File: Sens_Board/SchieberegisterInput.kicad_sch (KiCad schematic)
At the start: 18 parts, among them U4 74HC165

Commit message: Senssoard Firsat LAyout start
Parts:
- C10: renamed from C76; footprint Capacitor_SMD:C_0603_1608Metric -> Capacitor_SMD:C_0402_1005Metric
- C11: renamed from C88; footprint Capacitor_SMD:C_0603_1608Metric -> Capacitor_SMD:C_0402_1005Metric
- C12: renamed from C100; footprint Capacitor_SMD:C_0603_1608Metric -> Capacitor_SMD:C_0402_1005Metric
- C4: footprint Capacitor_SMD:C_0603_1608Metric -> Capacitor_SMD:C_0402_1005Metric
- C5: renamed from C16; footprint Capacitor_SMD:C_0603_1608Metric -> Capacitor_SMD:C_0402_1005Metric
- C6: renamed from C28; footprint Capacitor_SMD:C_0603_1608Metric -> Capacitor_SMD:C_0402_1005Metric
- C7: renamed from C40; footprint Capacitor_SMD:C_0603_1608Metric -> Capacitor_SMD:C_0402_1005Metric
- C8: renamed from C52; footprint Capacitor_SMD:C_0603_1608Metric -> Capacitor_SMD:C_0402_1005Metric
- C9: renamed from C64; footprint Capacitor_SMD:C_0603_1608Metric -> Capacitor_SMD:C_0402_1005Metric
- R25: renamed from R18; footprint Resistor_SMD:R_0603_1608Metric -> Resistor_SMD:R_0402_1005Metric
- R26: renamed from R19; footprint Resistor_SMD:R_0603_1608Metric -> Resistor_SMD:R_0402_1005Metric
- R27: renamed from R20; footprint Resistor_SMD:R_0603_1608Metric -> Resistor_SMD:R_0402_1005Metric
- R28: renamed from R21; footprint Resistor_SMD:R_0603_1608Metric -> Resistor_SMD:R_0402_1005Metric
- R29: renamed from R22; footprint Resistor_SMD:R_0603_1608Metric -> Resistor_SMD:R_0402_1005Metric
- R30: renamed from R23; footprint Resistor_SMD:R_0603_1608Metric -> Resistor_SMD:R_0402_1005Metric
- R31: renamed from R24; footprint Resistor_SMD:R_0603_1608Metric -> Resistor_SMD:R_0402_1005Metric
- R32: renamed from R25; footprint Resistor_SMD:R_0603_1608Metric -> Resistor_SMD:R_0402_1005Metric
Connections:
- net D0: now also C12.1
- net D1: now also C11.1
- net D2: now also C10.1
- net D3: now also C9.1
- net D4: now also C8.1
- net D5: now also C7.1
- net D6: now also C6.1
- net D7: now also C5.1

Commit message: set Komponents SensorBoard
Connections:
- net D0: now also C9.1, R29.2, U4.14 (D3); no longer C12.1, R32.2, U4.11 (D0)
- net D1: now also C10.1, R30.2, U4.13 (D2); no longer C11.1, R31.2, U4.12 (D1)
- net D2: now also C11.1, R31.2, U4.12 (D1); no longer C10.1, R30.2, U4.13 (D2)
- net D3: now also C12.1, R32.2, U4.11 (D0); no longer C9.1, R29.2, U4.14 (D3)
- net D4: now also C5.1, R25.2, U4.6 (D7); no longer C8.1, R28.2, U4.3 (D4)
- net D5: now also C6.1, R26.2, U4.5 (D6); no longer C7.1, R27.2, U4.4 (D5)
- net D6: now also C7.1, R27.2, U4.4 (D5); no longer C6.1, R26.2, U4.5 (D6)
- net D7: now also C8.1, R28.2, U4.3 (D4); no longer C5.1, R25.2, U4.6 (D7)
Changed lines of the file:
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@@
+	(wire
+		(pts
+			(xy 142.24 77.47) (xy 143.51 77.47)
+		)
+		(stroke
+			(width 0)
+			(type default)
+		)
+	)
 	(wire
 		(pts
@@
 	(wire
 		(pts
-			(xy 142.24 77.47) (xy 143.51 77.47)
-		)
-		(stroke
-			(width 0)
-			(type default)
-		)
-	)
-	(wire
-		(pts
 			(xy 143.51 55.88) (xy 149.86 55.88)
 		)
@@
 	(wire
 		(pts
+			(xy 135.89 80.01) (xy 137.16 80.01)
+		)
+		(stroke
+			(width 0)
+			(type default)
+		)
+	)
+	(wire
+		(pts
 			(xy 124.46 55.88) (xy 124.46 58.42)
 		)
@@
 	(wire
 		(pts
+			(xy 130.81 66.04) (xy 130.81 82.55)
+		)
+		(stroke
+			(width 0)
+			(type default)
+		)
+	)
+	(wire
+		(pts
+			(xy 129.54 82.55) (xy 130.81 82.55)
+		)
+		(stroke
+			(width 0)
+			(type default)
+		)
+	)
+	(wire
+		(pts
 			(xy 124.46 85.09) (xy 165.1 85.09)
 		)
@@
 	(wire
 		(pts
+			(xy 148.59 74.93) (xy 149.86 74.93)
+		)
+		(stroke
+			(width 0)
+			(type default)
+		)
+	)
+	(wire
+		(pts
+			(xy 102.87 92.71) (xy 105.41 92.71)
+		)
+		(stroke
+			(width 0)
+			(type default)
+		)
+	)
+	(wire
+		(pts
 			(xy 118.11 55.88) (xy 124.46 55.88)
 		)
@@
 	(wire
 		(pts
-			(xy 104.14 92.71) (xy 105.41 92.71)
-		)
-		(stroke
-			(width 0)
-			(type default)
-		)
-	)
-	(wire
-		(pts
 			(xy 177.8 53.34) (xy 177.8 54.61)
 		)
@@
 	(wire
 		(pts
-			(xy 135.89 80.01) (xy 137.16 80.01)
-		)
-		(stroke
-			(width 0)
-			(type default)
-		)
-	)
-	(wire
-		(pts
 			(xy 111.76 66.04) (xy 111.76 90.17)
 		)
@@
 	(wire
 		(pts
-			(xy 149.86 74.93) (xy 148.59 74.93)
-		)
-		(stroke
-			(width 0)
-			(type default)
-		)
-	)
-	(wire
-		(pts
 			(xy 130.81 82.55) (xy 165.1 82.55)
 		)
@@
 	(wire
 		(pts
-			(xy 129.54 82.55) (xy 130.81 82.55)
-		)
-		(stroke
-			(width 0)
-			(type default)
-		)
-	)
-	(wire
-		(pts
 			(xy 128.27 110.49) (xy 130.81 110.49)
 		)
@@
 	(wire
 		(pts
-			(xy 130.81 66.04) (xy 130.81 82.55)
-		)
-		(stroke
-			(width 0)
-			(type default)
-		)
-	)
-	(wire
-		(pts
 			(xy 124.46 85.09) (xy 124.46 99.06)
 		)
@@
 	(hierarchical_label "D7"
 		(shape input)
-		(at 104.14 92.71 180)
+		(at 123.19 85.09 180)
 		(effects
 			(font
@@
 	(hierarchical_label "D0"
 		(shape input)
+		(at 129.54 82.55 180)
+		(effects
+			(font
+				(size 1.27 1.27)
+			)
+			(justify right)
+		)
+	)
+	(hierarchical_label "D1"
+		(shape input)
+		(at 135.89 80.01 180)
+		(effects
+			(font
+				(size 1.27 1.27)
+			)
+			(justify right)
+		)
+	)
+	(hierarchical_label "D6"
+		(shape input)
+		(at 116.84 87.63 180)
+		(effects
+			(font
+				(size 1.27 1.27)
+			)
+			(justify right)
+		)
+	)
+	(hierarchical_label "D2"
+		(shape input)
+		(at 142.24 77.47 180)
+		(effects
+			(font
+				(size 1.27 1.27)
+			)
+			(justify right)
+		)
+	)
+	(hierarchical_label "D5"
+		(shape input)
+		(at 110.49 90.17 180)
+		(effects
+			(font
+				(size 1.27 1.27)
+			)
+			(justify right)
+		)
+	)
+	(hierarchical_label "D4"
+		(shape input)
+		(at 102.87 92.71 180)
+		(effects
+			(font
+				(size 1.27 1.27)
+			)
+			(justify right)
+		)
+	)
+	(hierarchical_label "Out"
+		(shape input)
+		(at 193.04 72.39 0)
+		(effects
+			(font
+				(size 1.27 1.27)
+			)
+			(justify left)
+		)
+	)
+	(hierarchical_label "In"
+		(shape input)
+		(at 162.56 72.39 180)
+		(effects
+			(font
+				(size 1.27 1.27)
+			)
+			(justify right)
+		)
+	)
+	(hierarchical_label "D3"
+		(shape input)
 		(at 148.59 74.93 180)
 		(effects
 			(font
-				(size 1.27 1.27)
-			)
-			(justify right)
-		)
-	)
-	(hierarchical_label "D1"
-		(shape input)
-		(at 142.24 77.47 180)
-		(effects
-			(font
-				(size 1.27 1.27)
-			)
-			(justify right)
-		)
-	)
-	(hierarchical_label "D6"
-		(shape input)
-		(at 110.49 90.17 180)
-		(effects
-			(font
-				(size 1.27 1.27)
-			)
-			(justify right)
-		)
-	)
-	(hierarchical_label "D2"
-		(shape input)
-		(at 135.89 80.01 180)
-		(effects
-			(font
-				(size 1.27 1.27)
-			)
-			(justify right)
-		)
-	)
-	(hierarchical_label "D5"
-		(shape input)
-		(at 116.84 87.63 180)
-		(effects
-			(font
-				(size 1.27 1.27)
-			)
-			(justify right)
-		)
-	)
-	(hierarchical_label "D4"
-		(shape input)
-		(at 123.19 85.09 180)
-		(effects
-			(font
-				(size 1.27 1.27)
-			)
-			(justify right)
-		)
-	)
-	(hierarchical_label "Out"
-		(shape input)
-		(at 193.04 72.39 0)
-		(effects
-			(font
-				(size 1.27 1.27)
-			)
-			(justify left)
-		)
-	)
-	(hierarchical_label "In"
-		(shape input)
-		(at 162.56 72.39 180)
-		(effects
-			(font
-				(size 1.27 1.27)
-			)
-			(justify right)
-		)
-	)
-	(hierarchical_label "D3"
-		(shape input)
-		(at 129.54 82.55 180)
-		(effects
-			(font

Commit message: finish SensBoard
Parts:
- removed C10, C11, C12, C5, C6, C7, C8, C9: 100n, Capacitor_SMD:C_0402_1005Metric, symbol Device:C

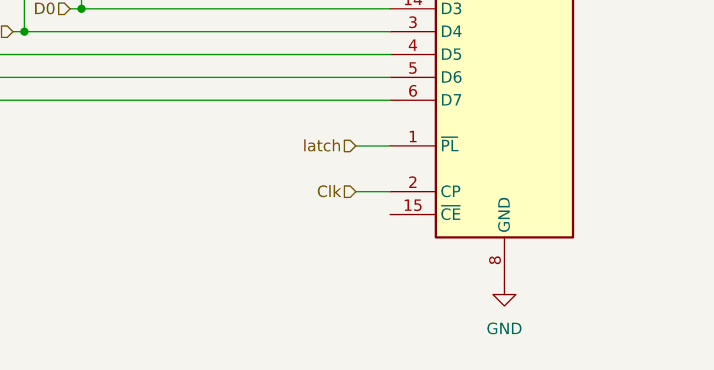
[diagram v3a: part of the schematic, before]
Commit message: add pull UP/DOWN
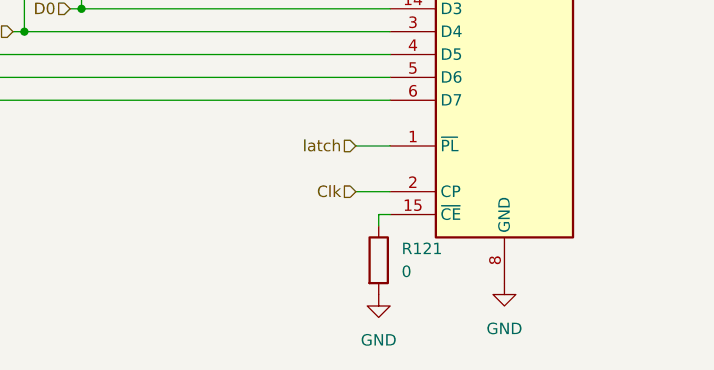
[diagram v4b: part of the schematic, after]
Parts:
- added R121: 0, Resistor_SMD:R_0402_1005Metric, symbol Device:R
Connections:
- net GND: now also R121.2
- net at U4.15 (~{CE}): now also R121.1

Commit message: fixes and optmierung
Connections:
- net D0: now also R32.2, U4.11 (D0); no longer R29.2, U4.14 (D3)
- net D1: now also R31.2, U4.12 (D1); no longer R30.2, U4.13 (D2)
- net D2: now also R30.2, U4.13 (D2); no longer R31.2, U4.12 (D1)
- net D3: now also R29.2, U4.14 (D3); no longer R32.2, U4.11 (D0)
- net D4: now also R28.2, U4.3 (D4); no longer R25.2, U4.6 (D7)
- net D5: now also R27.2, U4.4 (D5); no longer R26.2, U4.5 (D6)
- net D6: now also R26.2, U4.5 (D6); no longer R27.2, U4.4 (D5)
- net D7: now also R25.2, U4.6 (D7); no longer R28.2, U4.3 (D4)
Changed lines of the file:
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@@
 	(hierarchical_label "D7"
 		(shape input)
-		(at 123.19 85.09 180)
+		(at 102.87 92.71 180)
 		(effects
 			(font
@@
 	(hierarchical_label "D0"
 		(shape input)
-		(at 129.54 82.55 180)
+		(at 148.59 74.93 180)
 		(effects
 			(font
@@
 	(hierarchical_label "D1"
 		(shape input)
-		(at 135.89 80.01 180)
+		(at 142.24 77.47 180)
 		(effects
 			(font
@@
 	(hierarchical_label "D6"
 		(shape input)
-		(at 116.84 87.63 180)
+		(at 110.49 90.17 180)
 		(effects
 			(font
@@
 	(hierarchical_label "D2"
 		(shape input)
-		(at 142.24 77.47 180)
+		(at 135.89 80.01 180)
 		(effects
 			(font
@@
 	(hierarchical_label "D5"
 		(shape input)
-		(at 110.49 90.17 180)
+		(at 116.84 87.63 180)
 		(effects
 			(font
@@
 	(hierarchical_label "D4"
 		(shape input)
-		(at 102.87 92.71 180)
+		(at 123.19 85.09 180)
 		(effects
 			(font
@@
 	(hierarchical_label "D3"
 		(shape input)
-		(at 148.59 74.93 180)
+		(at 129.54 82.55 180)
 		(effects
 			(font
